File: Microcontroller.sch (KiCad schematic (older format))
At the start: 12 parts, among them J1 3220-10-0100-00, J2 4POS_2MM, U1 ATSAMD11D14A-MUT

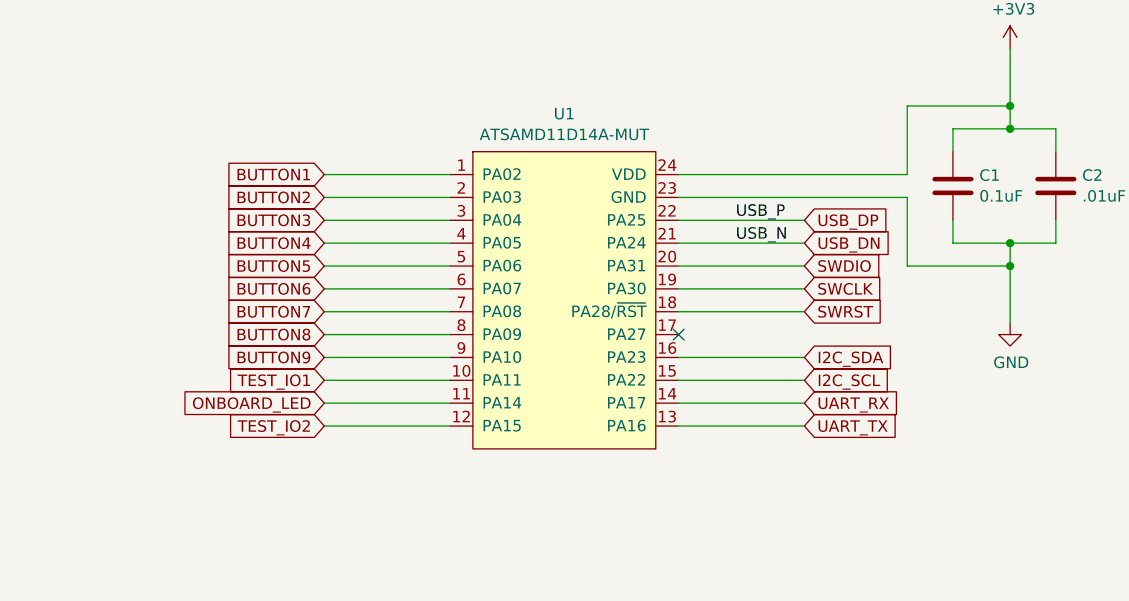
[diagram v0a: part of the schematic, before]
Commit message: Initial layout complete. Pins moved to make layout easy
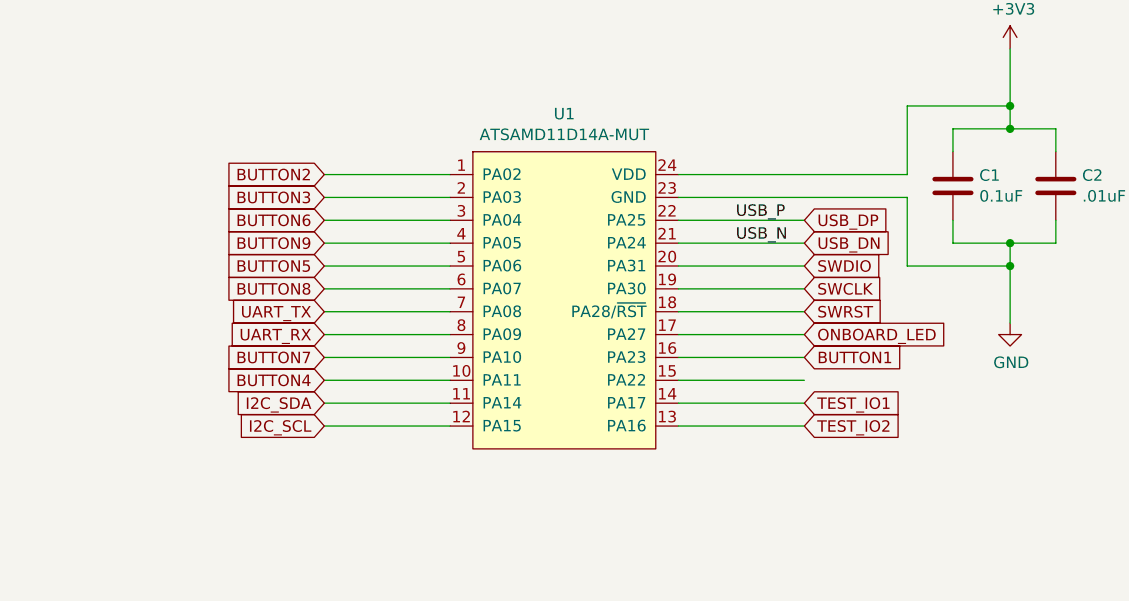
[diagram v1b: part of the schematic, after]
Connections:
- net BUTTON1: now also U1.16 (PA23); no longer U1.1 (PA02)
- net BUTTON2: now also U1.1 (PA02); no longer U1.2 (PA03)
- net BUTTON3: now also U1.2 (PA03); no longer U1.3 (PA04)
- net BUTTON4: now also U1.10 (PA11); no longer U1.4 (PA05)
- net BUTTON6: now also U1.3 (PA04); no longer U1.6 (PA07)
- net BUTTON7: now also U1.9 (PA10); no longer U1.7 (PA08)
- net BUTTON8: now also U1.6 (PA07); no longer U1.8 (PA09)
- net BUTTON9: now also U1.4 (PA05); no longer U1.9 (PA10)
- net I2C_SCL: now also U1.12 (PA15); no longer U1.15 (PA22)
- net I2C_SDA: now also U1.11 (PA14); no longer U1.16 (PA23)
- net ONBOARD_LED: now also U1.17 (PA27); no longer U1.11 (PA14)
- net TEST_IO1: now also U1.14 (PA17); no longer U1.10 (PA11)
- net TEST_IO2: now also U1.13 (PA16); no longer U1.12 (PA15)
- net UART_RX: now also U1.8 (PA09); no longer U1.14 (PA17)
- net UART_TX: now also U1.7 (PA08); no longer U1.13 (PA16)
- no-connect marks 3 -> 2
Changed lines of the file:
@@
 Wire Wire Line
 	6350 3950 5800 3950
+Text GLabel 4250 4350 0    50   Input ~ 0
+I2C_SDA
+Text GLabel 4250 4450 0    50   Input ~ 0
+I2C_SCL
+Wire Wire Line
+	5800 4150 6350 4150
+Wire Wire Line
+	6350 4250 5800 4250
+Text GLabel 4250 4050 0    50   Input ~ 0
+UART_RX
+Text GLabel 4250 3950 0    50   Input ~ 0
+UART_TX
+Wire Wire Line
+	6350 4350 5800 4350
+Wire Wire Line
+	6350 4450 5800 4450
 Text GLabel 6350 4150 2    50   Input ~ 0
-I2C_SDA
-Text GLabel 6350 4250 2    50   Input ~ 0
-I2C_SCL
-Wire Wire Line
-	5800 4150 6350 4150
-Wire Wire Line
-	6350 4250 5800 4250
-Text GLabel 6350 4350 2    50   Input ~ 0
-UART_RX
-Text GLabel 6350 4450 2    50   Input ~ 0
-UART_TX
-Wire Wire Line
-	6350 4350 5800 4350
-Wire Wire Line
-	6350 4450 5800 4450
+BUTTON1
+Wire Wire Line
+	4800 3350 4250 3350
 Text GLabel 4250 3350 0    50   Input ~ 0
-BUTTON1
-Wire Wire Line
-	4800 3350 4250 3350
+BUTTON2
 Text GLabel 4250 3450 0    50   Input ~ 0
-BUTTON2
-Text GLabel 4250 3550 0    50   Input ~ 0
 BUTTON3
-Text GLabel 4250 3650 0    50   Input ~ 0
+Text GLabel 4250 4250 0    50   Input ~ 0
 BUTTON4
 Text GLabel 4250 3750 0    50   Input ~ 0
 BUTTON5
+Text GLabel 4250 3550 0    50   Input ~ 0
+BUTTON6
+Text GLabel 4250 4150 0    50   Input ~ 0
+BUTTON7
 Text GLabel 4250 3850 0    50   Input ~ 0
-BUTTON6
-Text GLabel 4250 3950 0    50   Input ~ 0
-BUTTON7
-Text GLabel 4250 4050 0    50   Input ~ 0
 BUTTON8
-Text GLabel 4250 4150 0    50   Input ~ 0
+Text GLabel 4250 3650 0    50   Input ~ 0
 BUTTON9
 Wire Wire Line
@@
 Wire Wire Line
 	4250 3450 4800 3450
-NoConn ~ 5800 4050
-Text GLabel 4250 4350 0    50   Input ~ 0
+Text GLabel 6350 4050 2    50   Input ~ 0
 ONBOARD_LED
 Wire Wire Line
@@
 Text Notes 1350 5750 0    50   ~ 0
 UART CONNECTOR
-Text GLabel 4250 4250 0    50   Input ~ 0
+Text GLabel 6350 4350 2    50   Input ~ 0
 TEST_IO1
-Text GLabel 4250 4450 0    50   Input ~ 0
+Text GLabel 6350 4450 2    50   Input ~ 0
 TEST_IO2
 Wire Wire Line
@@
 Text Notes 3400 5650 0    50   ~ 0
 EXTRA TEST IO PULLDOWNS
+Wire Wire Line
+	6350 4050 5800 4050
 $EndSCHEMATC
